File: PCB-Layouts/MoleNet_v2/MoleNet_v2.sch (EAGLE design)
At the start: 31 parts, among them IC1 25LC080P, Q1 BS250, Q2 BS170, U1 MCP1703-5002E/DB, U2 ATMEGA328P-PU, U3 RFM69CW, X1 SMA-142-0711-821/826

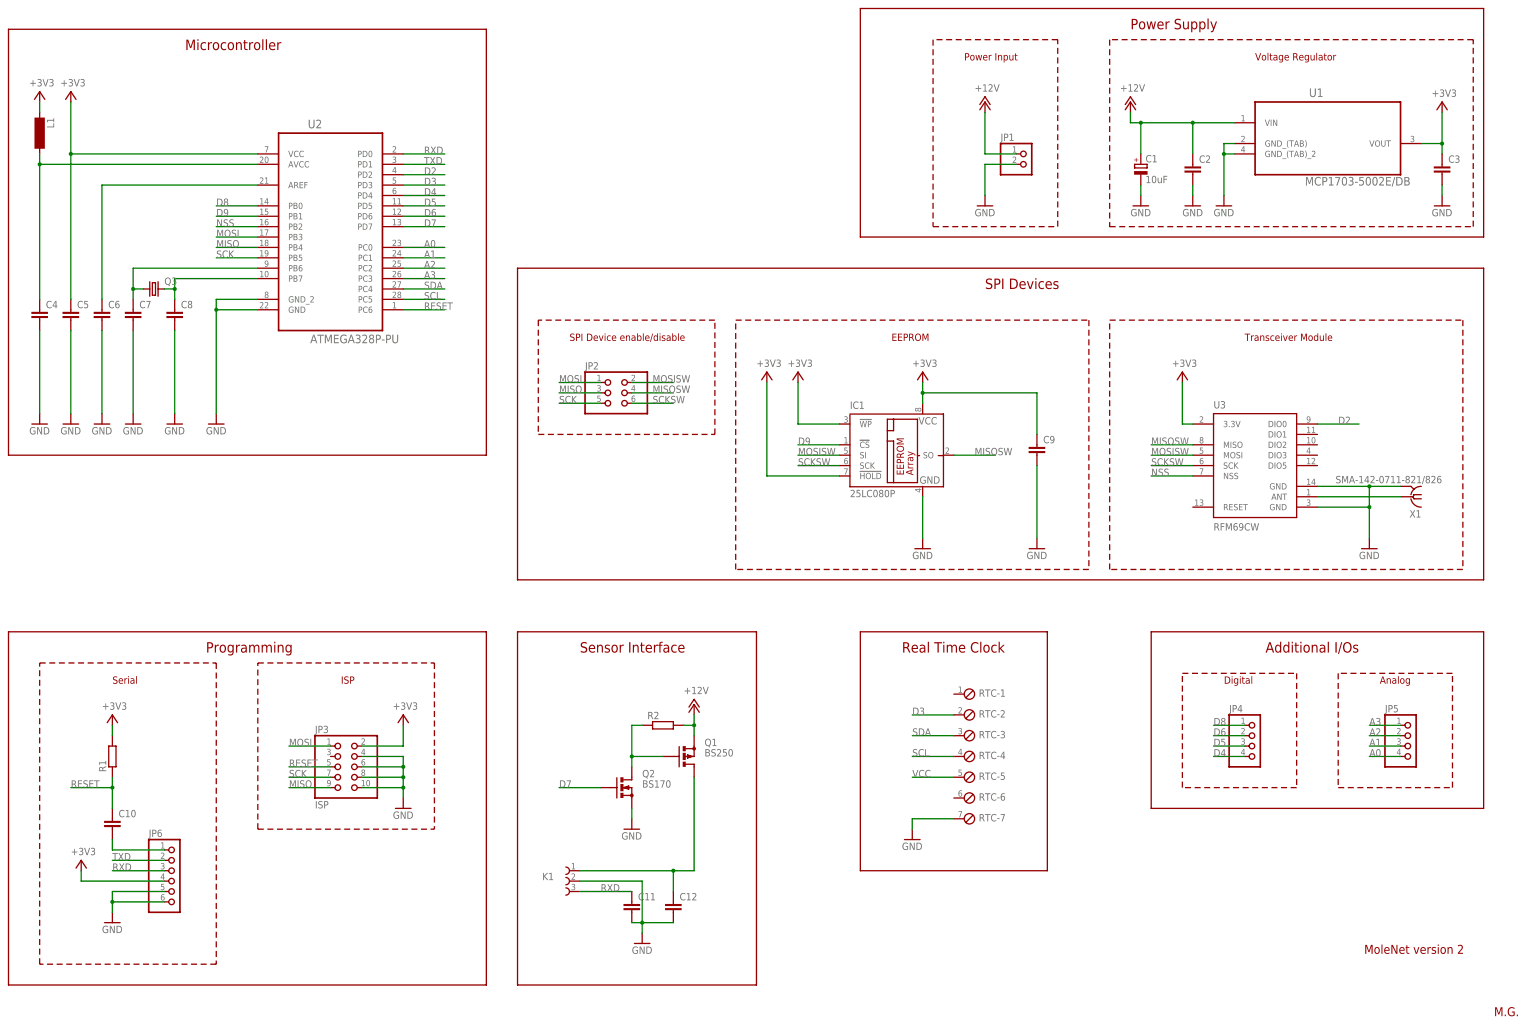
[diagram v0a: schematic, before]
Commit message: added/corrected part values in all layouts; created partlist for version 2.1
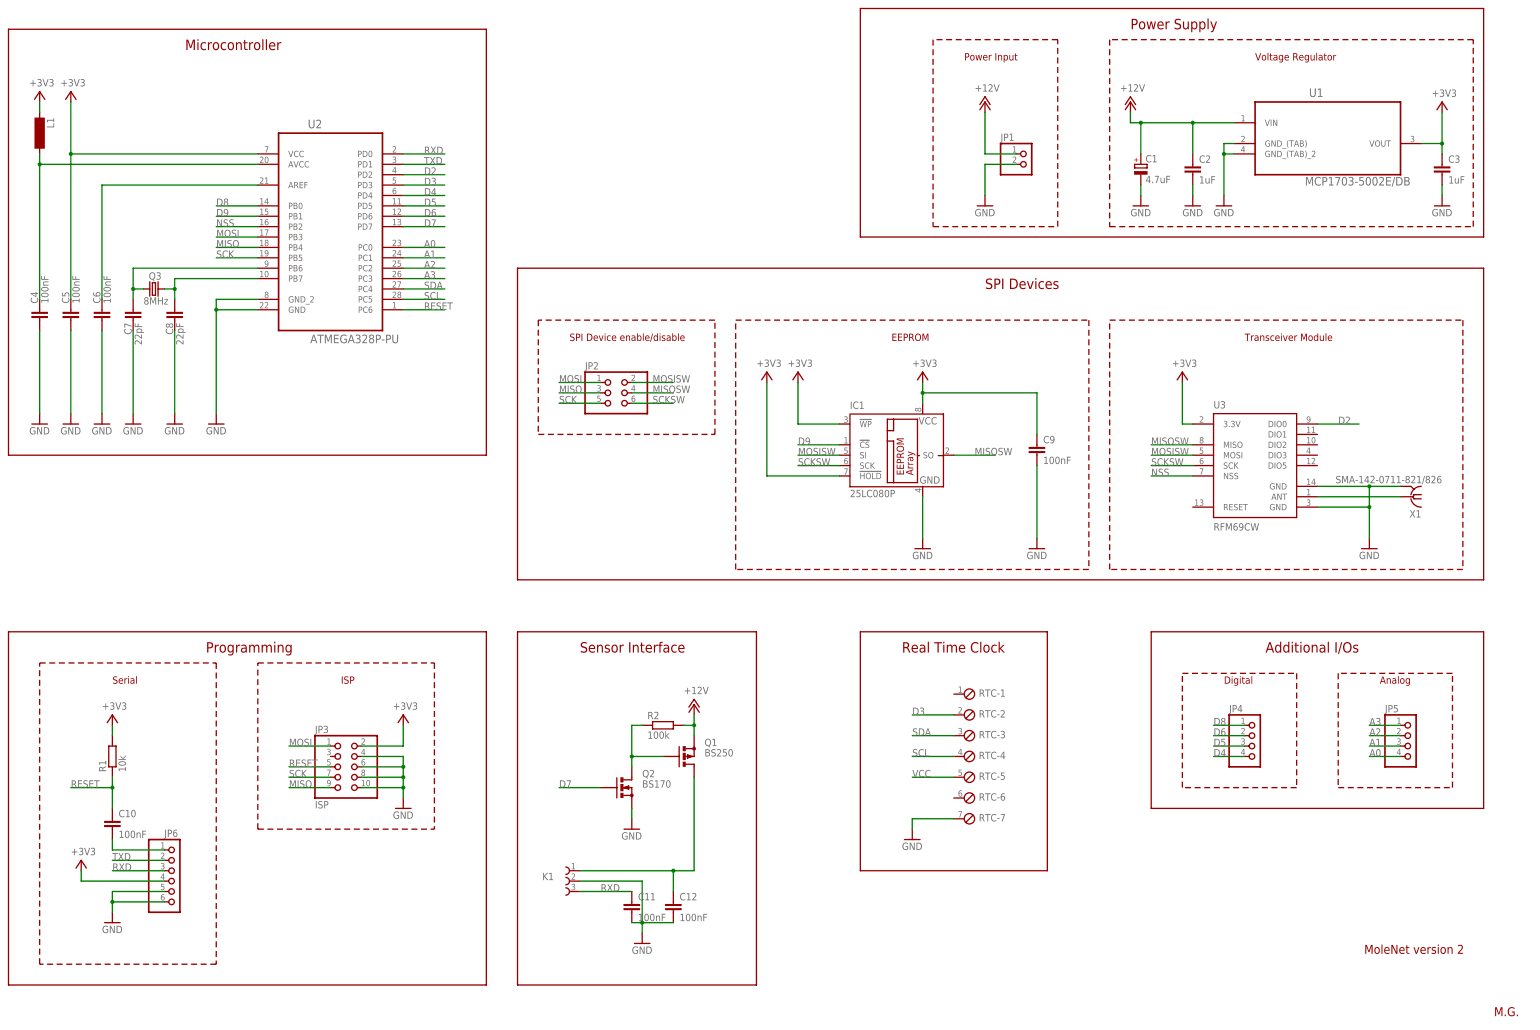
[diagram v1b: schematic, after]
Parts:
- C1: value 10uF -> 4.7uF
- C10, C11, C12, C4, C5, C6, C9: value (none) -> 100nF
- C2, C3: value (none) -> 1uF
- C7, C8: value (none) -> 22pF
- Q3: value (none) -> 8MHz
- R1: value (none) -> 10k
- R2: value (none) -> 100k
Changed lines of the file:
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@@
 <part name="Q1" library="transistor-small-signal" deviceset="BS250" device=""/>
 <part name="GND1" library="supply1" deviceset="GND" device=""/>
-<part name="R2" library="resistor" deviceset="R-EU_" device="0207/10"/>
+<part name="R2" library="resistor" deviceset="R-EU_" device="0207/10" value="100k"/>
 <part name="+3V1" library="supply1" deviceset="+3V3" device=""/>
 <part name="GND2" library="supply1" deviceset="GND" device=""/>
 <part name="L1" library="inductor-neosid" deviceset="BS" device="11"/>
-<part name="C1" library="resistor" deviceset="CPOL-EU" device="E2.5-6" value="10uF"/>
-<part name="C2" library="resistor" deviceset="C-EU" device="025-025X050"/>
-<part name="C3" library="resistor" deviceset="C-EU" device="025-025X050"/>
-<part name="C4" library="resistor" deviceset="C-EU" device="025-025X050"/>
+<part name="C1" library="resistor" deviceset="CPOL-EU" device="E2.5-6" value="4.7uF"/>
+<part name="C2" library="resistor" deviceset="C-EU" device="025-025X050" value="1uF"/>
+<part name="C3" library="resistor" deviceset="C-EU" device="025-025X050" value="1uF"/>
+<part name="C4" library="resistor" deviceset="C-EU" device="025-025X050" value="100nF"/>
 <part name="GND3" library="supply1" deviceset="GND" device=""/>
-<part name="C6" library="resistor" deviceset="C-EU" device="025-025X050"/>
+<part name="C6" library="resistor" deviceset="C-EU" device="025-025X050" value="100nF"/>
 <part name="GND4" library="supply1" deviceset="GND" device=""/>
 <part name="+3V2" library="supply1" deviceset="+3V3" device=""/>
@@
 <part name="GND12" library="supply1" deviceset="GND" device=""/>
 <part name="FRAME1" library="frames" deviceset="A3L-LOC" device=""/>
-<part name="C5" library="resistor" deviceset="C-EU" device="025-025X050"/>
+<part name="C5" library="resistor" deviceset="C-EU" device="025-025X050" value="100nF"/>
 <part name="GND13" library="supply1" deviceset="GND" device=""/>
 <part name="JP6" library="pinhead" deviceset="PINHD-1X6" device=""/>
 <part name="GND14" library="supply1" deviceset="GND" device=""/>
 <part name="+3V8" library="supply1" deviceset="+3V3" device=""/>
-<part name="C10" library="resistor" deviceset="C-EU" device="025-025X050"/>
-<part name="R1" library="resistor" deviceset="R-EU_" device="0207/10"/>
+<part name="C10" library="resistor" deviceset="C-EU" device="025-025X050" value="100nF"/>
+<part name="R1" library="resistor" deviceset="R-EU_" device="0207/10" value="10k"/>
 <part name="+3V9" library="supply1" deviceset="+3V3" device=""/>
-<part name="Q3" library="crystal" deviceset="CRYSTAL" device="HC18U-V"/>
-<part name="C7" library="resistor" deviceset="C-EU" device="025-025X050"/>
-<part name="C8" library="resistor" deviceset="C-EU" device="025-025X050"/>
+<part name="Q3" library="crystal" deviceset="CRYSTAL" device="HC18U-V" value="8MHz"/>
+<part name="C7" library="resistor" deviceset="C-EU" device="025-025X050" value="22pF"/>
+<part name="C8" library="resistor" deviceset="C-EU" device="025-025X050" value="22pF"/>
 <part name="GND16" library="supply1" deviceset="GND" device=""/>
 <part name="GND17" library="supply1" deviceset="GND" device=""/>
@@
 <part name="GND18" library="supply1" deviceset="GND" device=""/>
 <part name="+3V10" library="supply1" deviceset="+3V3" device=""/>
-<part name="C9" library="resistor" deviceset="C-EU" device="025-025X050"/>
+<part name="C9" library="resistor" deviceset="C-EU" device="025-025X050" value="100nF"/>
 <part name="GND19" library="supply1" deviceset="GND" device=""/>
-<part name="C11" library="resistor" deviceset="C-EU" device="025-025X050"/>
-<part name="C12" library="resistor" deviceset="C-EU" device="025-025X050"/>
+<part name="C11" library="resistor" deviceset="C-EU" device="025-025X050" value="100nF"/>
+<part name="C12" library="resistor" deviceset="C-EU" device="025-025X050" value="100nF"/>
 <part name="JP2" library="pinhead" deviceset="PINHD-2X3" device=""/>
 <part name="JP5" library="pinhead" deviceset="PINHD-1X4" device=""/>
@@
 <instance part="C2" gate="G$1" x="302.26" y="213.36"/>
 <instance part="C3" gate="G$1" x="363.22" y="213.36"/>
-<instance part="C4" gate="G$1" x="20.32" y="177.8"/>
+<instance part="C4" gate="G$1" x="20.32" y="177.8" smashed="yes">
+<attribute name="NAME" x="19.939" y="179.324" size="1.778" layer="95" rot="R90"/>
+<attribute name="VALUE" x="22.479" y="179.324" size="1.778" layer="96" rot="R90"/>
+</instance>
 <instance part="GND3" gate="1" x="20.32" y="149.86"/>
-<instance part="C6" gate="G$1" x="35.56" y="177.8"/>
+<instance part="C6" gate="G$1" x="35.56" y="177.8" smashed="yes">
+<attribute name="NAME" x="35.179" y="179.324" size="1.778" layer="95" rot="R90"/>
+<attribute name="VALUE" x="37.719" y="179.324" size="1.778" layer="96" rot="R90"/>
+</instance>
 <instance part="GND4" gate="1" x="35.56" y="149.86"/>
 <instance part="+3V2" gate="G$1" x="27.94" y="231.14" smashed="yes">
@@
 <instance part="GND12" gate="1" x="309.88" y="203.2"/>
 <instance part="FRAME1" gate="G$1" x="0" y="0"/>
-<instance part="C5" gate="G$1" x="27.94" y="177.8"/>
+<instance part="C5" gate="G$1" x="27.94" y="177.8" smashed="yes">
+<attribute name="NAME" x="27.559" y="179.324" size="1.778" layer="95" rot="R90"/>
+<attribute name="VALUE" x="30.099" y="179.324" size="1.778" layer="96" rot="R90"/>
+</instance>
 <instance part="GND13" gate="1" x="27.94" y="149.86"/>
-<instance part="JP6" gate="A" x="53.34" y="38.1"/>
+<instance part="JP6" gate="A" x="53.34" y="38.1" smashed="yes">
+<attribute name="NAME" x="50.8" y="48.895" size="1.778" layer="95"/>
+<attribute name="VALUE" x="46.99" y="27.94" size="1.778" layer="96"/>
+</instance>
 <instance part="GND14" gate="1" x="38.1" y="27.94"/>
 <instance part="+3V8" gate="G$1" x="30.48" y="43.18" smashed="yes">
@@
 <attribute name="VALUE" x="35.56" y="80.01" size="1.778" layer="96"/>
 </instance>
-<instance part="Q3" gate="G$1" x="48.26" y="182.88"/>
-<instance part="C7" gate="G$1" x="43.18" y="177.8"/>
-<instance part="C8" gate="G$1" x="53.34" y="177.8"/>
+<instance part="Q3" gate="G$1" x="48.26" y="182.88" smashed="yes">
+<attribute name="NAME" x="46.99" y="185.166" size="1.778" layer="95"/>
+<attribute name="VALUE" x="45.72" y="179.07" size="1.778" layer="96"/>
+</instance>
+<instance part="C7" gate="G$1" x="43.18" y="177.8" smashed="yes">
+<attribute name="NAME" x="42.799" y="171.704" size="1.778" layer="95" rot="R90"/>
+<attribute name="VALUE" x="45.339" y="169.164" size="1.778" layer="96" rot="R90"/>
+</instance>
+<instance part="C8" gate="G$1" x="53.34" y="177.8" smashed="yes">
+<attribute name="NAME" x="52.959" y="171.704" size="1.778" layer="95" rot="R90"/>
+<attribute name="VALUE" x="55.499" y="169.164" size="1.778" layer="96" rot="R90"/>
+</instance>
 <instance part="GND16" gate="1" x="43.18" y="149.86"/>
 <instance part="GND17" gate="1" x="53.34" y="149.86"/>
